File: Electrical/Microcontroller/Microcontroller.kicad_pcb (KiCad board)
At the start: 2 copper layers, 26 x 30 mm, 34 parts, among them J1 JST SH 1x4, J2 Conn_01x10, J3 Conn_ARM_JTAG_SWD_10, J4 Conn_02x06_Odd_Even, P1 USB_C_Plug_USB2.0, SW1 RESET, U1 ATSAMD21E18A-M, U2 GD25Q16CT, U3 AP2112K-3.3, U4 TLV70036_SOT23-5

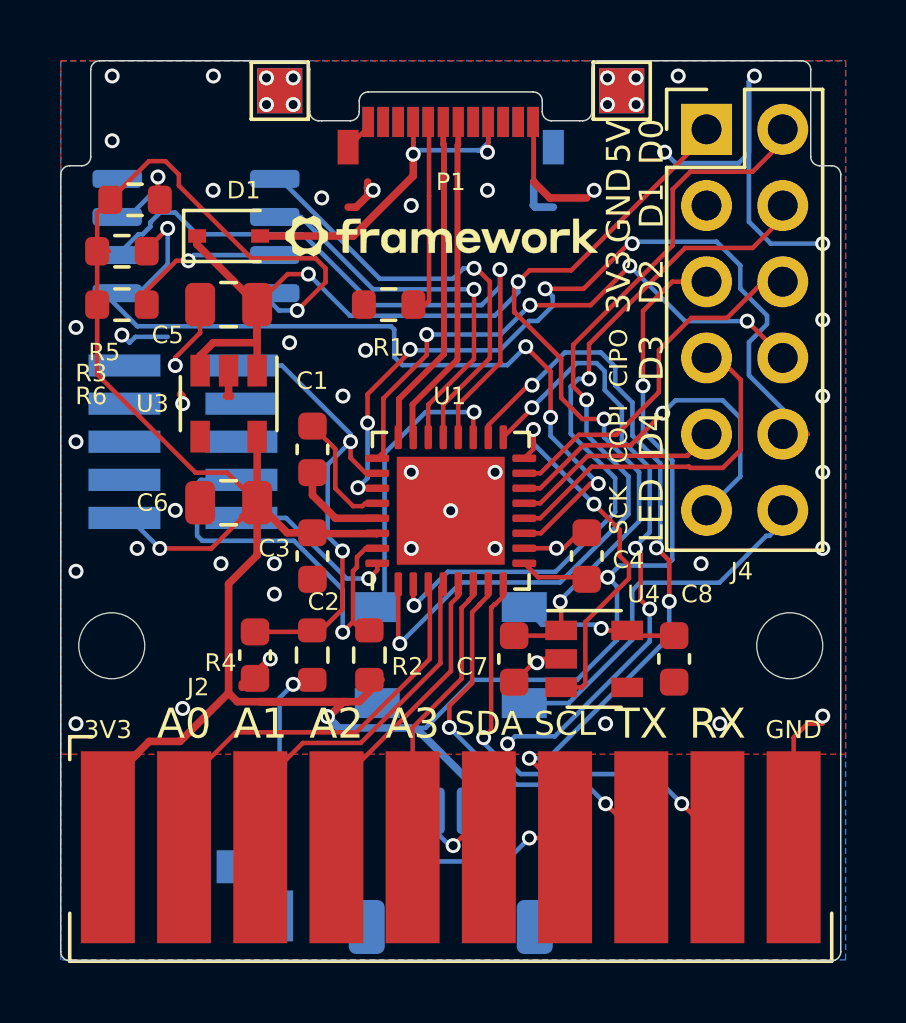
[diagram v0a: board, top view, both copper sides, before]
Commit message: Fixed designators and clarified footprint of D2.
I did change the C2 and R4 designators since they were mixed up. 
I also did modify the footprint of D2 to make it more obvious how to orient it since usually pin 1 is marked on the physical package but for that LED it's pin 3.
Also updated the files to KiCad 7.
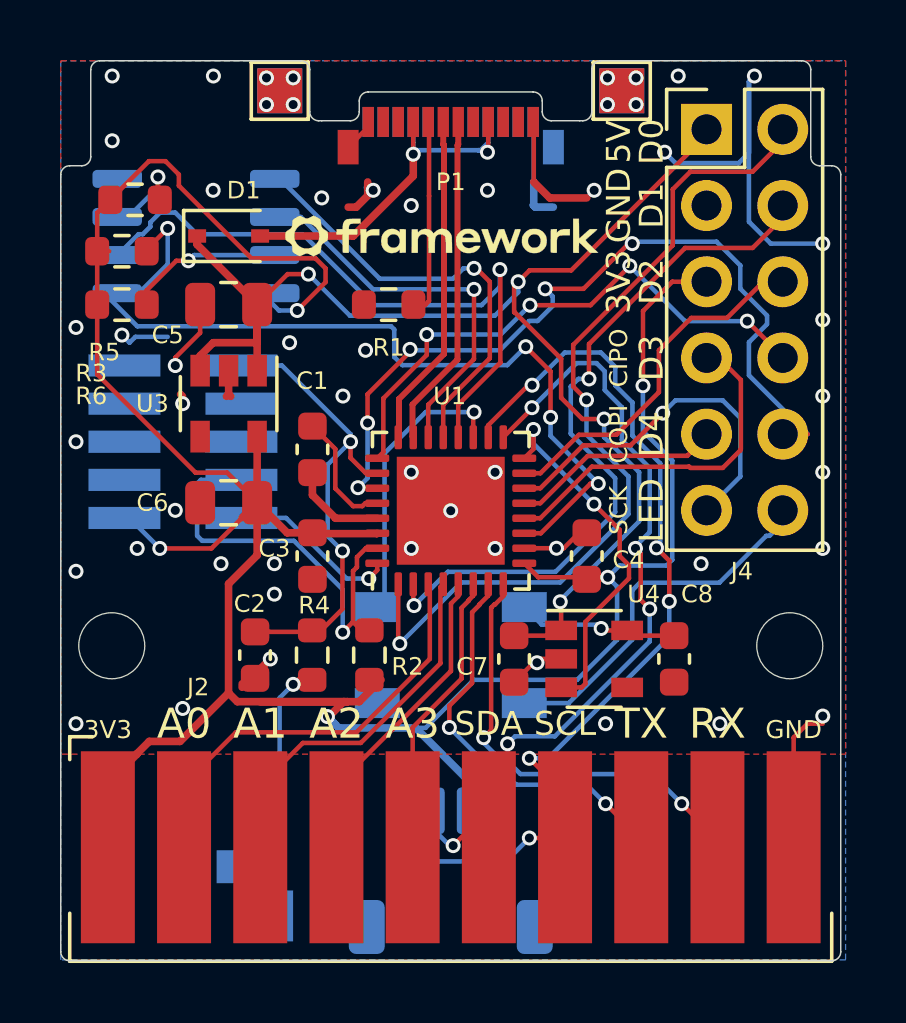
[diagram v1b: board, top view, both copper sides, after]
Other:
- net class Default removed
